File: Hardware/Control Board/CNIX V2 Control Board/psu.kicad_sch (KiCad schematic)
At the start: 37 parts, among them Q100 MMBTA42, Q101 FDS2734, U100 UCC3803

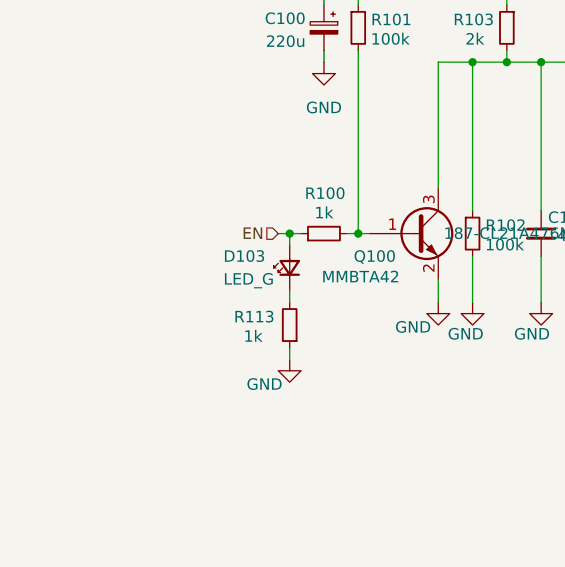
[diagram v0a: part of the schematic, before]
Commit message: control board: added ht-psu enable jumper
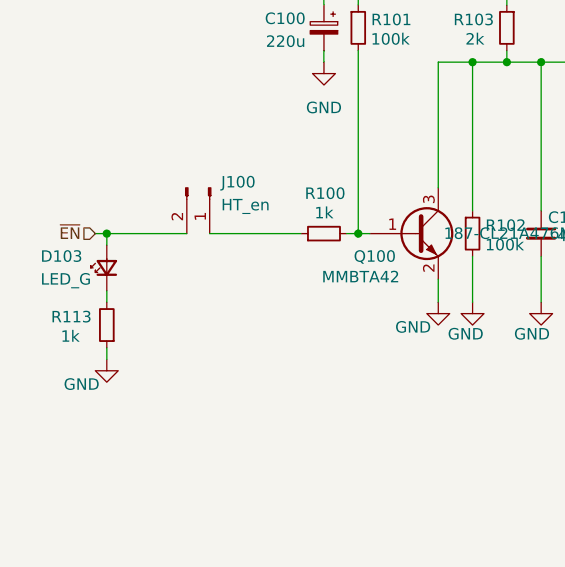
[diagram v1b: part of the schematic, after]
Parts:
- added J100: HT_en, Connector_PinHeader_2.54mm:PinHeader_1x02_P2.54mm_Vertical, symbol Connector:Conn_01x02_Pin
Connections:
- net EN: no longer names the net of R100.1
- net EN: now also J100.1 (Pin_1); no longer D103.2 (A)
- new net ~{EN}: D103.2 (A), J100.2 (Pin_2)
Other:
- moved on the sheet: D103, R113
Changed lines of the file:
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@@
 	)
 	(junction
-		(at 76.2 97.79)
+		(at 55.88 97.79)
 		(diameter 0)
 		(color 0 0 0 0)
@@
 	(wire
 		(pts
+			(xy 67.31 97.79) (xy 77.47 97.79)
+		)
+		(stroke
+			(width 0)
+			(type default)
+		)
+	)
+	(wire
+		(pts
 			(xy 207.01 80.01) (xy 210.82 80.01)
 		)
@@
 	(wire
 		(pts
-			(xy 76.2 104.14) (xy 76.2 105.41)
+			(xy 55.88 104.14) (xy 55.88 105.41)
 		)
 		(stroke
@@
 	(wire
 		(pts
-			(xy 76.2 97.79) (xy 77.47 97.79)
+			(xy 55.88 97.79) (xy 64.77 97.79)
 		)
 		(stroke
@@
 	(wire
 		(pts
-			(xy 76.2 110.49) (xy 76.2 111.76)
+			(xy 55.88 110.49) (xy 55.88 111.76)
 		)
 		(stroke
@@
 	(wire
 		(pts
-			(xy 74.93 97.79) (xy 76.2 97.79)
+			(xy 54.61 97.79) (xy 55.88 97.79)
 		)
 		(stroke
@@
 	(wire
 		(pts
-			(xy 76.2 97.79) (xy 76.2 99.06)
+			(xy 55.88 97.79) (xy 55.88 99.06)
 		)
 		(stroke
@@
 		)
 	)
-	(hierarchical_label "EN"
+	(hierarchical_label "~{EN}"
 		(shape input)
-		(at 74.93 97.79 180)
+		(at 54.61 97.79 180)
 		(effects
 			(font
@@
 	(symbol
 		(lib_id "Device:LED_Small")
-		(at 76.2 101.6 90)
+		(at 55.88 101.6 90)
 		(unit 1)
 		(exclude_from_sim no)
@@
 		(dnp no)
 		(property "Reference" "D103"
-			(at 68.834 100.33 90)
+			(at 48.514 100.33 90)
 			(effects
 				(font
@@
 		)
 		(property "Value" "LED_G"
-			(at 68.834 102.87 90)
+			(at 48.514 102.87 90)
 			(effects
 				(font
@@
 		)
 		(property "Footprint" "LED_SMD:LED_0805_2012Metric"
-			(at 76.2 101.6 90)
+			(at 55.88 101.6 90)
 			(effects
 				(font
@@
 		)
 		(property "Datasheet" "~"
-			(at 76.2 101.6 90)
+			(at 55.88 101.6 90)
 			(effects
 				(font
@@
 		)
 		(property "Description" "Light emitting diode, small symbol"
-			(at 76.2 101.6 0)
+			(at 55.88 101.6 0)
 			(effects
 				(font
@@
 		)
 		(property "Mouser URL" ""
-			(at 76.2 101.6 0)
+			(at 55.88 101.6 0)
 			(effects
 				(font
@@
 		)
 		(property "Mouser Nr." ""
-			(at 76.2 101.6 0)
+			(at 55.88 101.6 0)
 			(effects
 				(font
@@
 		)
 		(property "Mouser-Nr." ""
-			(at 76.2 101.6 0)
+			(at 55.88 101.6 0)
 			(effects
 				(font
@@
 		)
 		(property "Reichelt-Nr." ""
-			(at 76.2 101.6 0)
+			(at 55.88 101.6 0)
 			(effects
 				(font
@@
 	(symbol
 		(lib_id "power:GND")
-		(at 76.2 111.76 0)
+		(at 55.88 111.76 0)
 		(unit 1)
 		(exclude_from_sim no)
@@
 		(dnp no)
 		(property "Reference" "#PWR0119"
-			(at 76.2 118.11 0)
+			(at 55.88 118.11 0)
 			(effects
 				(font
@@
 		)
 		(property "Value" "GND"
-			(at 73.406 114.554 0)
+			(at 53.086 114.554 0)
 			(effects
 				(font
@@
 		)
 		(property "Footprint" ""
-			(at 76.2 111.76 0)
+			(at 55.88 111.76 0)
 			(effects
 				(font
@@
 		)
 		(property "Datasheet" ""
-			(at 76.2 111.76 0)
+			(at 55.88 111.76 0)
 			(effects
 				(font
@@
 		)
 		(property "Description" "Power symbol creates a global label with name \"GND\" , ground"
-			(at 76.2 111.76 0)
+			(at 55.88 111.76 0)
 			(effects
 				(font
@@
 	)
 	(symbol
+		(lib_id "Connector:Conn_01x02_Pin")
+		(at 67.31 92.71 270)
+		(unit 1)
+		(exclude_from_sim no)
+		(in_bom yes)
+		(on_board yes)
+		(dnp no)
+		(fields_autoplaced yes)
+		(property "Reference" "J100"
+			(at 68.58 92.0749 90)
+			(effects
+				(font
+					(size 1.27 1.27)
+				)
+				(justify left)
+			)
+		)
+		(property "Value" "HT_en"
+			(at 68.58 94.6149 90)
+			(effects
+				(font
+					(size 1.27 1.27)
+				)
+				(justify left)
+			)
+		)
+		(property "Footprint" "Connector_PinHeader_2.54mm:PinHeader_1x02_P2.54mm_Vertical"
+			(at 67.31 92.71 0)
+			(effects
+				(font
+					(size 1.27 1.27)
+				)
+				(hide yes)
+			)
+		)
+		(property "Datasheet" "~"
+			(at 67.31 92.71 0)
+			(effects
+				(font
+					(size 1.27 1.27)
+				)
+				(hide yes)
+			)
+		)
+		(property "Description" "Generic connector, single row, 01x02, script generated"
+			(at 67.31 92.71 0)
+			(effects
+				(font
+					(size 1.27 1.27)
+				)
+				(hide yes)
+			)
+		)
+		(pin "2"
+		)
+		(pin "1"
+		)
+		(instances
+			(project ""
+				(path "/552fdcf9-00a6-4d96-ad8b-ee11dd6b40ba/9c594c2f-787f-4f16-953b-7a7d40f29933"
+					(reference "J100")
+					(unit 1)
+				)
+			)
+		)
+	)
+	(symbol
 		(lib_id "power:GND")
 		(at 175.26 105.41 0)
@@
 	(symbol
 		(lib_id "Device:R_Small")
-		(at 76.2 107.95 180)
+		(at 55.88 107.95 180)
 		(unit 1)
 		(exclude_from_sim no)
@@
 		(dnp no)
 		(property "Reference" "R113"
-			(at 72.263 107.061 0)
+			(at 51.943 107.061 0)
 			(effects
 				(font
@@
 		)
 		(property "Value" "1k"
-			(at 72.136 109.22 0)
+			(at 51.816 109.22 0)
 			(effects
 				(font
@@
 		)
 		(property "Footprint" "Resistor_SMD:R_0805_2012Metric_Pad1.20x1.40mm_HandSolder"
-			(at 76.2 107.95 0)
+			(at 55.88 107.95 0)
 			(effects
 				(font
@@
 		)
 		(property "Datasheet" "~"
-			(at 76.2 107.95 0)
+			(at 55.88 107.95 0)
 			(effects
 				(font
@@
 		)
 		(property "Description" "Resistor, small symbol"
-			(at 76.2 107.95 0)
+			(at 55.88 107.95 0)
 			(effects
 				(font
@@
 		)
 		(property "Mouser-Nr." ""
-			(at 76.2 107.95 0)
+			(at 55.88 107.95 0)
 			(effects
 				(font
@@
 		)
 		(property "Reichelt-Nr." ""
-			(at 76.2 107.95 0)
+			(at 55.88 107.95 0)
 			(effects
 				(font

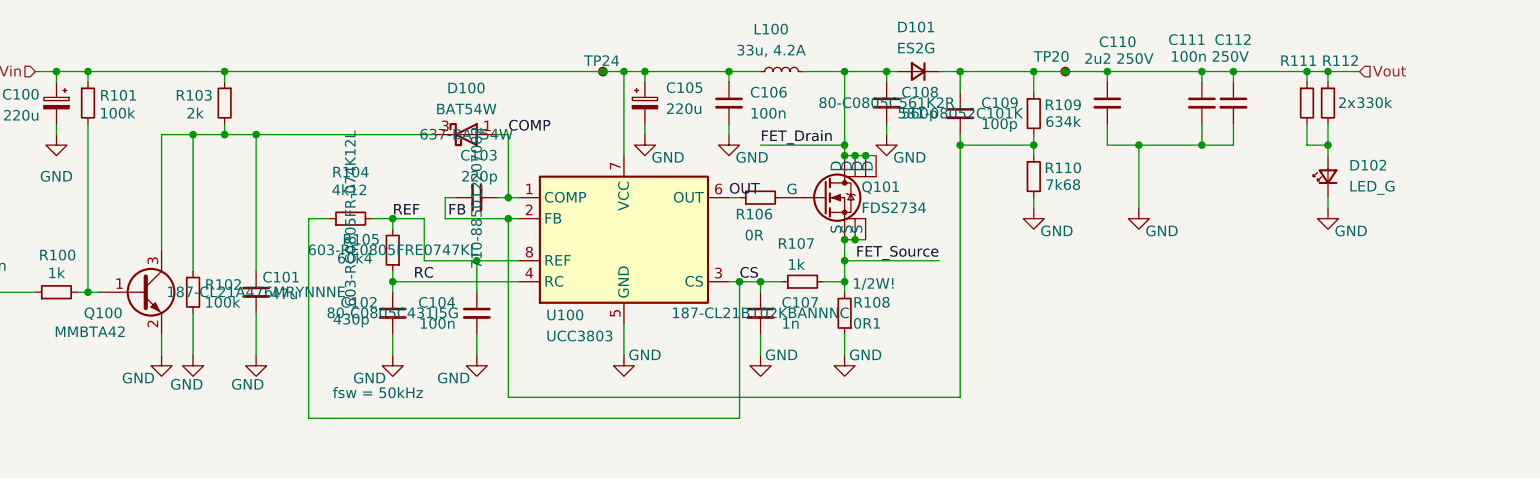
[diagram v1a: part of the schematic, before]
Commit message: finalized V2 and cleaned up Silkscreen
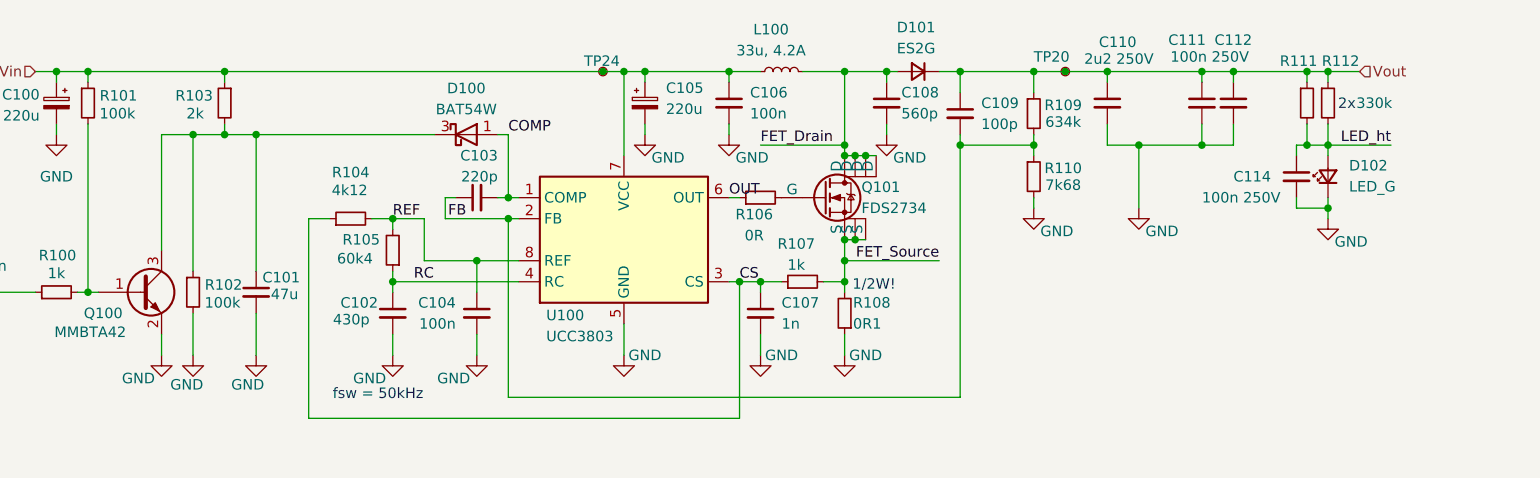
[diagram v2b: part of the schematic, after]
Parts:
- added C114: 100n 250V, Capacitor_SMD:C_0805_2012Metric_Pad1.18x1.45mm_HandSolder, symbol Device:C_Small
- C110: Mouser Nr. 810-CGA4J3X7T2E104MA -> 710-885342214003; Mouser URL (none) -> https://www.mouser.de/ProductDetail/Wurth-Elektronik/885342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
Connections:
- net GND: now also C114.2
- net LED_ht: now reaches D102.2 (A), R111.2, R112.2
- net LED_ht: now also C114.1
